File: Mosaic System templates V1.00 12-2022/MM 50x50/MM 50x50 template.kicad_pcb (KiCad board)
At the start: 2 copper layers, 50 x 50 mm, 3 parts

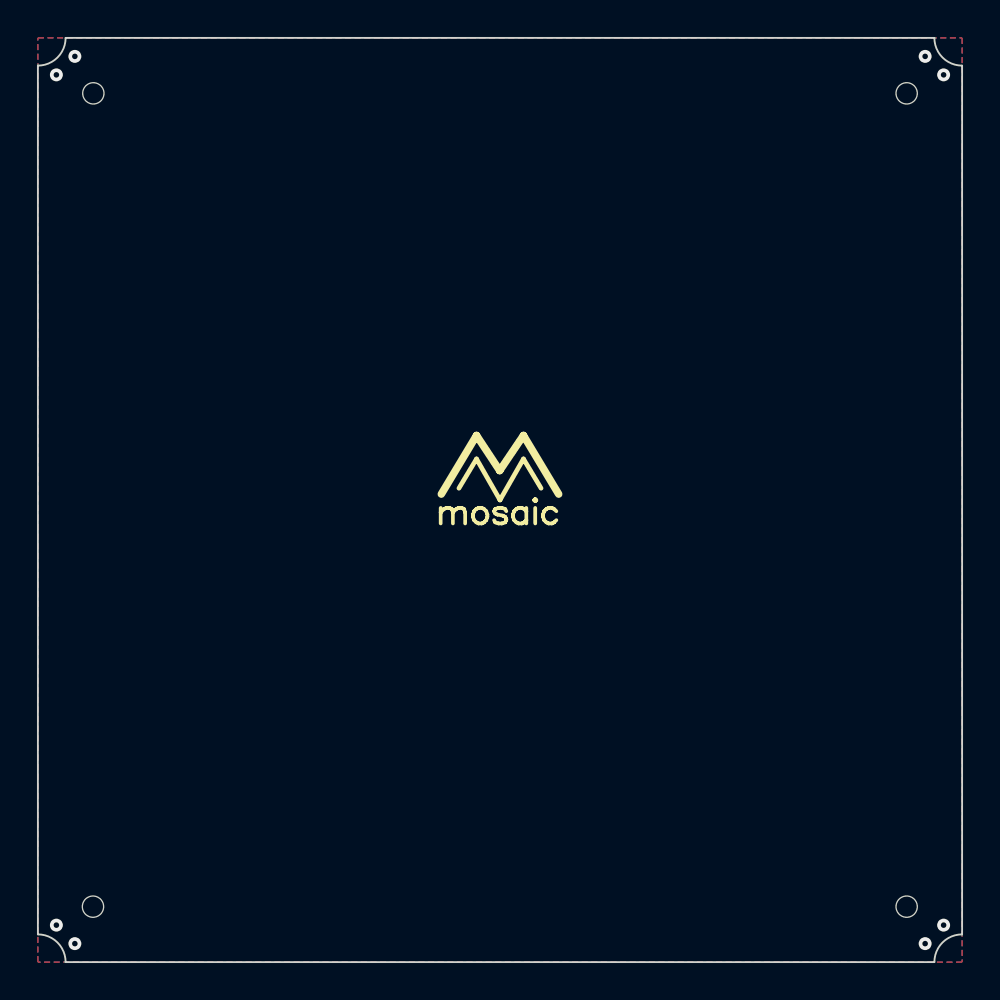
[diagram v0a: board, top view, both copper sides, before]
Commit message: V1.1
Clean up of some redundant footprints and added the correct polygons for the keepout area of the corners.
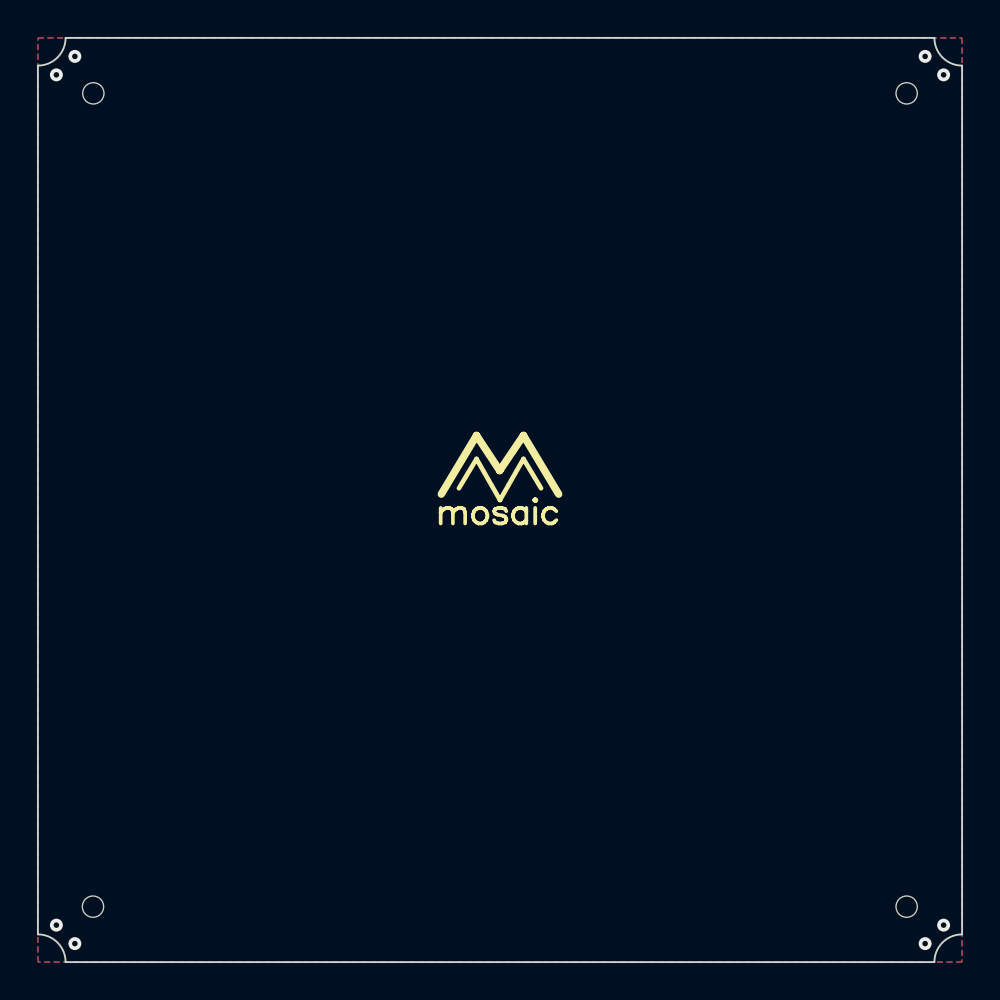
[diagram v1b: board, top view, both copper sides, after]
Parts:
- moved REF4 10.0 mm to (150.0, 120.0)

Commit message: update templates
Updated templates now have the current polygons for the soldermask keepout area and restrict any traces or components from entering those areas
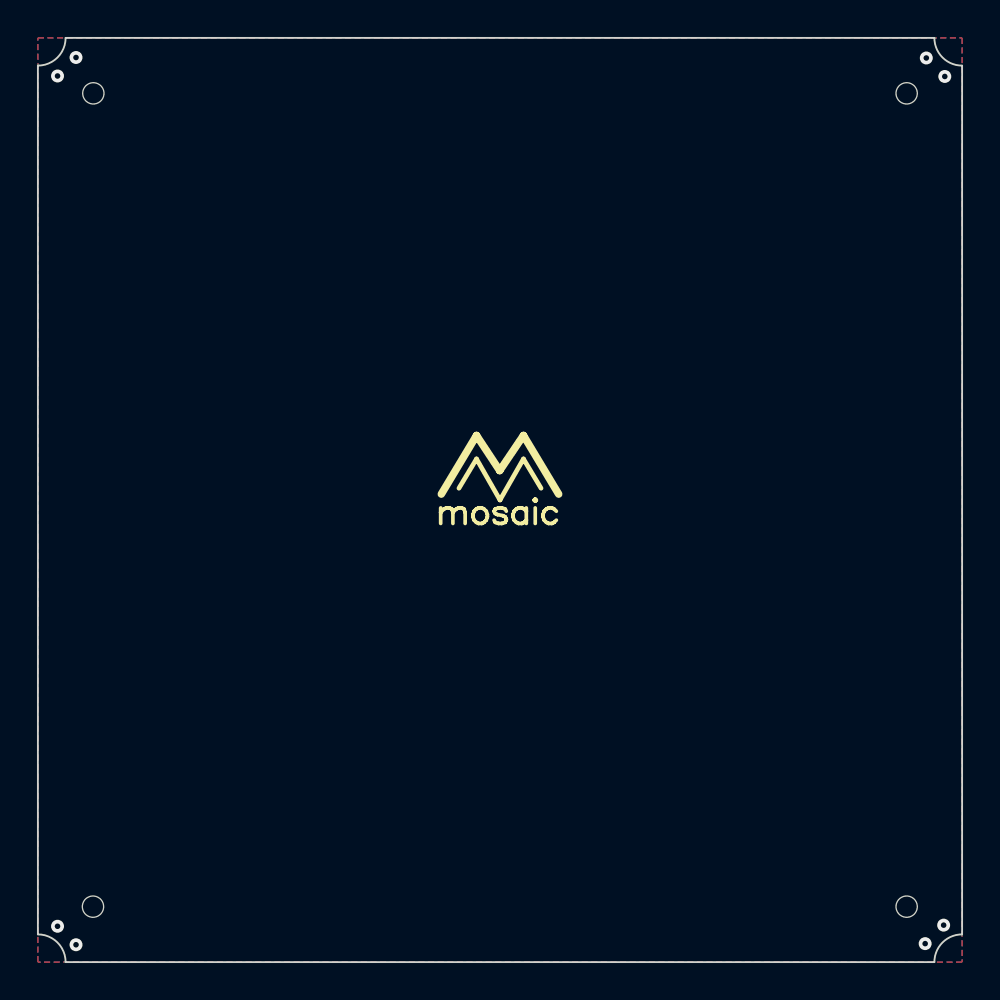
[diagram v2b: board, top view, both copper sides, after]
